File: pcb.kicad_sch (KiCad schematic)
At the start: 23 parts, among them SW1 SW_Push, SW2 SW_Push, U1 Pico

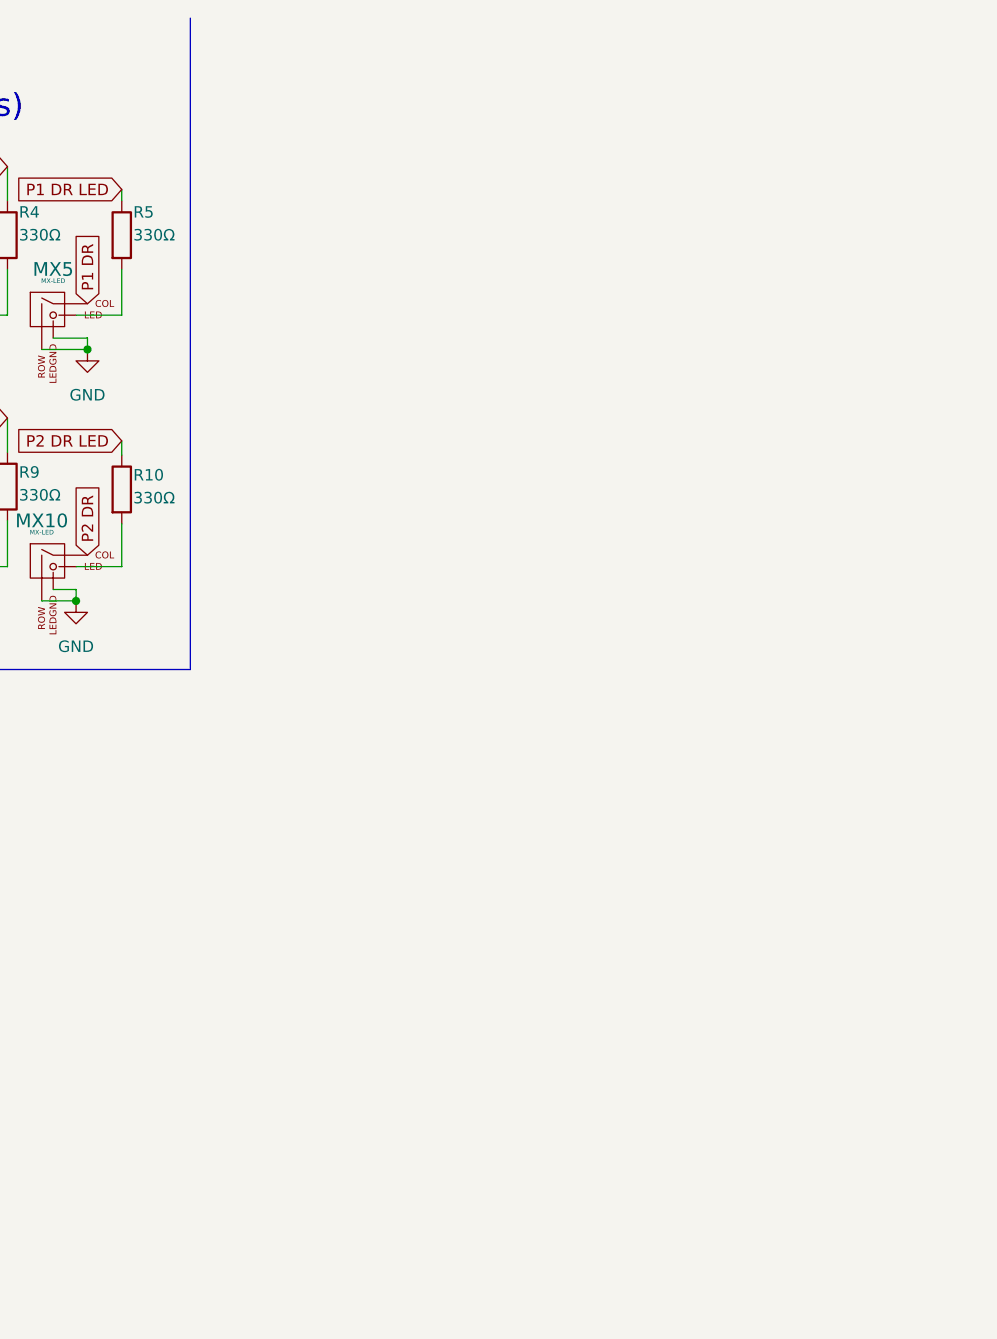
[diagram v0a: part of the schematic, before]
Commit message: Add WS2812B footprints, various tweaks
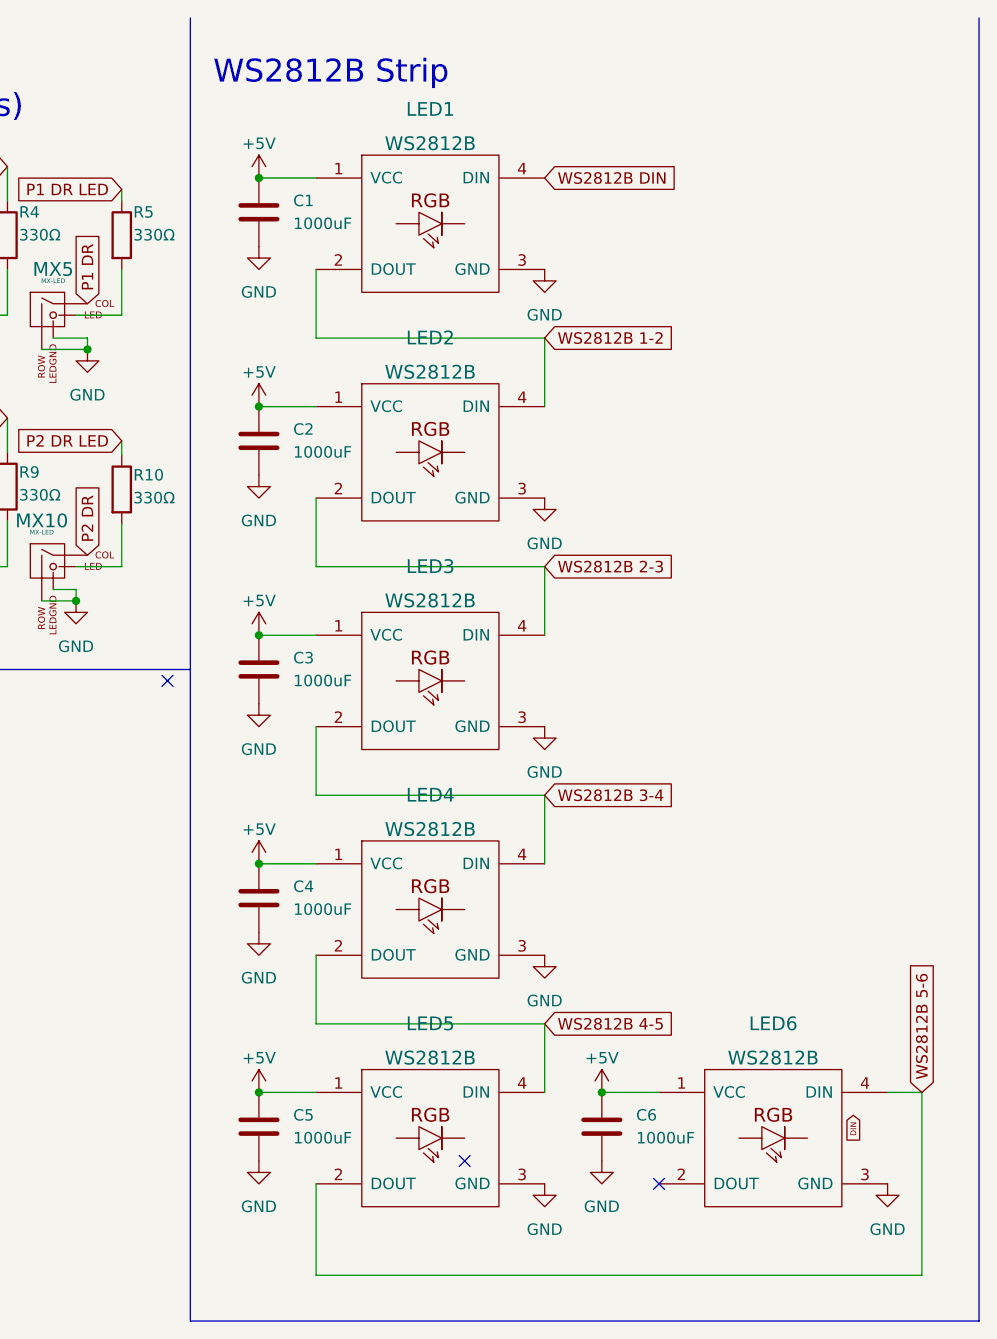
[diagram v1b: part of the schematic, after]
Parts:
- added C1, C2, C3, C4, C5, C6: 1000uF, Capacitor_SMD:C_0805_2012Metric_Pad1.18x1.45mm_HandSolder, symbol Device:C
- added LED1, LED2, LED3, LED4, LED5, LED6: WS2812B, LED_SMD:LED_WS2812B_PLCC4_5.0x5.0mm_P3.2mm, symbol ws2812b:WS2812B
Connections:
- net +5V: now also C1.1, C2.1, C3.1, C4.1, C5.1, C6.1, LED1.1 (VCC), LED2.1 (VCC), LED3.1 (VCC), LED4.1 (VCC), LED5.1 (VCC), LED6.1 (VCC)
- net GND: now also C1.2, C2.2, C3.2, C4.2, C5.2, C6.2, LED1.3 (GND), LED2.3 (GND), LED3.3 (GND), LED4.3 (GND), LED5.3 (GND), LED6.3 (GND)
- net WS2812B DIN: now also LED1.4 (DIN)
- new net WS2812B 1-2: LED1.2 (DOUT), LED2.4 (DIN)
- new net WS2812B 2-3: LED2.2 (DOUT), LED3.4 (DIN)
- new net WS2812B 3-4: LED3.2 (DOUT), LED4.4 (DIN)
- new net WS2812B 4-5: LED4.2 (DOUT), LED5.4 (DIN)
- new net WS2812B 5-6: LED5.2 (DOUT), LED6.4 (DIN)
- no-connect marks 13 -> 16
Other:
- note added: "WS2812B Strip"

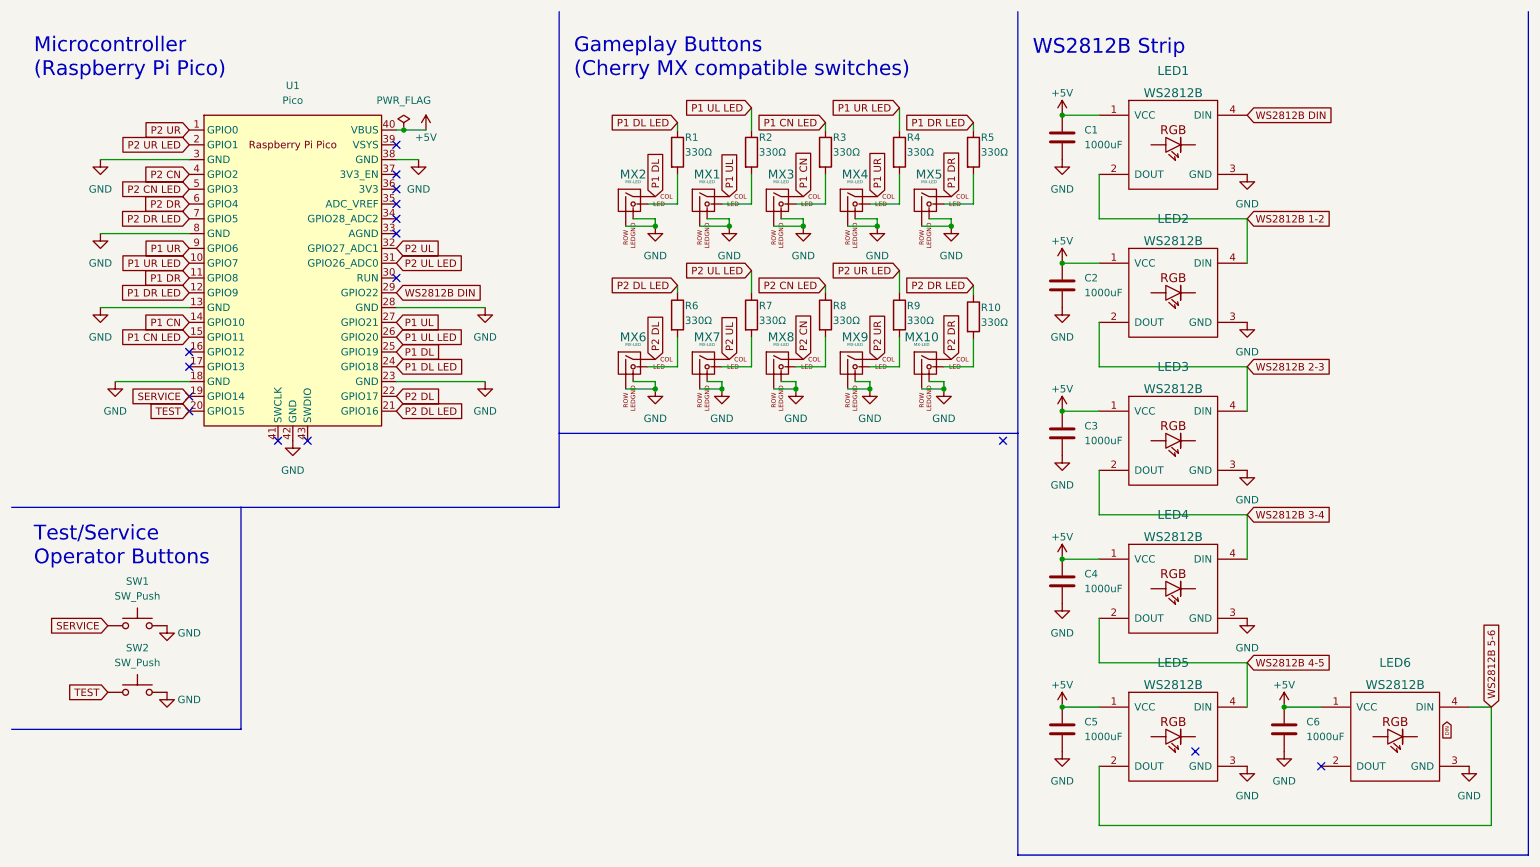
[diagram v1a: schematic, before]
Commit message: Fix P1 UL/DL being swapped
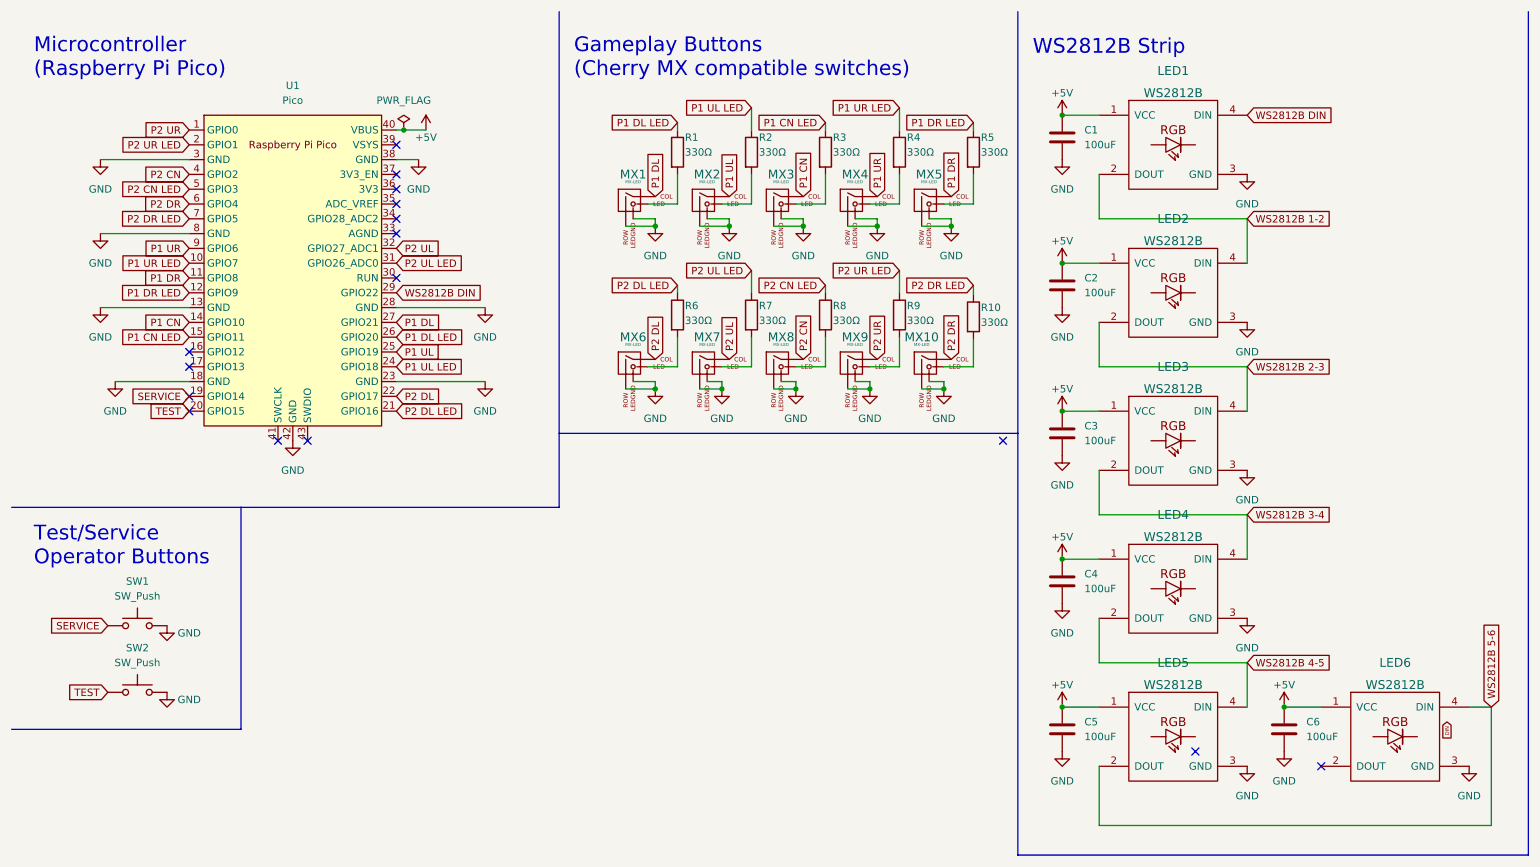
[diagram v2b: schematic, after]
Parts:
- C1, C2, C3, C4, C5, C6: value 1000uF -> 100uF
- LED1, LED2, LED3, LED4, LED5, LED6: LCSC (none) -> C2761795
- R1, R10, R2, R3, R4, R5, R6, R7, R8, R9: LCSC (none) -> C17630
- renumbered MX2 to MX1, MX1 to MX2
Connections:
- net P1 DL: now also U1.27 (GPIO21); no longer U1.25 (GPIO19)
- net P1 DL LED: now also U1.26 (GPIO20); no longer U1.24 (GPIO18)
- net P1 UL: now also U1.25 (GPIO19); no longer U1.27 (GPIO21)
- net P1 UL LED: now also U1.24 (GPIO18); no longer U1.26 (GPIO20)

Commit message: Add keeb.io Alps+Choc+MX footprint
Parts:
- MX1, MX10, MX2, MX3, MX4, MX5, MX6, MX7, MX8, MX9: footprint MX_Only:MXOnly-1U -> Keebio-Parts:MX-Alps-Choc-1U
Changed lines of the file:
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@@
       (effects (font (size 0.508 0.508)))
     )
-    (property "Footprint" "MX_Only:MXOnly-1U" (id 2) (at 126.365 43.815 0)
+    (property "Footprint" "Keebio-Parts:MX-Alps-Choc-1U" (id 2) (at 126.365 43.815 0)
       (effects (font (size 1.524 1.524)) hide)
     )
@@
       (effects (font (size 0.508 0.508)))
     )
-    (property "Footprint" "MX_Only:MXOnly-1U" (id 2) (at 113.665 71.755 0)
+    (property "Footprint" "Keebio-Parts:MX-Alps-Choc-1U" (id 2) (at 113.665 71.755 0)
       (effects (font (size 1.524 1.524)) hide)
     )
@@
       (effects (font (size 0.508 0.508)))
     )
-    (property "Footprint" "MX_Only:MXOnly-1U" (id 2) (at 139.065 71.755 0)
+    (property "Footprint" "Keebio-Parts:MX-Alps-Choc-1U" (id 2) (at 139.065 71.755 0)
       (effects (font (size 1.524 1.524)) hide)
     )
@@
       (effects (font (size 0.508 0.508)))
     )
-    (property "Footprint" "MX_Only:MXOnly-1U" (id 2) (at 151.765 43.815 0)
+    (property "Footprint" "Keebio-Parts:MX-Alps-Choc-1U" (id 2) (at 151.765 43.815 0)
       (effects (font (size 1.524 1.524)) hide)
     )
@@
       (effects (font (size 0.508 0.508)))
     )
-    (property "Footprint" "MX_Only:MXOnly-1U" (id 2) (at 113.665 43.815 0)
+    (property "Footprint" "Keebio-Parts:MX-Alps-Choc-1U" (id 2) (at 113.665 43.815 0)
       (effects (font (size 1.524 1.524)) hide)
     )
@@
       (effects (font (size 0.508 0.508)))
     )
-    (property "Footprint" "MX_Only:MXOnly-1U" (id 2) (at 139.065 43.815 0)
+    (property "Footprint" "Keebio-Parts:MX-Alps-Choc-1U" (id 2) (at 139.065 43.815 0)
       (effects (font (size 1.524 1.524)) hide)
     )
@@
       (effects (font (size 0.508 0.508)))
     )
-    (property "Footprint" "MX_Only:MXOnly-1U" (id 2) (at 100.965 71.755 0)
+    (property "Footprint" "Keebio-Parts:MX-Alps-Choc-1U" (id 2) (at 100.965 71.755 0)
       (effects (font (size 1.524 1.524)) hide)
     )
@@
       (effects (font (size 0.508 0.508)))
     )
-    (property "Footprint" "MX_Only:MXOnly-1U" (id 2) (at 100.965 43.815 0)
+    (property "Footprint" "Keebio-Parts:MX-Alps-Choc-1U" (id 2) (at 100.965 43.815 0)
       (effects (font (size 1.524 1.524)) hide)
     )
@@
       (effects (font (size 0.508 0.508)))
     )
-    (property "Footprint" "MX_Only:MXOnly-1U" (id 2) (at 151.765 71.755 0)
+    (property "Footprint" "Keebio-Parts:MX-Alps-Choc-1U" (id 2) (at 151.765 71.755 0)
       (effects (font (size 1.524 1.524)) hide)
     )
@@
       (effects (font (size 0.508 0.508)))
     )
-    (property "Footprint" "MX_Only:MXOnly-1U" (id 2) (at 126.365 71.755 0)
+    (property "Footprint" "Keebio-Parts:MX-Alps-Choc-1U" (id 2) (at 126.365 71.755 0)
       (effects (font (size 1.524 1.524)) hide)
     )
@@
     )
     (path "/9b58b2b3-67cf-495f-b667-1ffb1ad1d5b8"
-      (reference "MX1") (unit 1) (value "MX-LED") (footprint "MX_Only:MXOnly-1U")
+      (reference "MX1") (unit 1) (value "MX-LED") (footprint "Keebio-Parts:MX-Alps-Choc-1U")
     )
     (path "/766fdfb3-db19-48c2-b779-b910c8a2ecfb"
-      (reference "MX2") (unit 1) (value "MX-LED") (footprint "MX_Only:MXOnly-1U")
+      (reference "MX2") (unit 1) (value "MX-LED") (footprint "Keebio-Parts:MX-Alps-Choc-1U")
     )
     (path "/0a212509-b99d-4c27-a7b8-116754ebdf67"
-      (reference "MX3") (unit 1) (value "MX-LED") (footprint "MX_Only:MXOnly-1U")
+      (reference "MX3") (unit 1) (value "MX-LED") (footprint "Keebio-Parts:MX-Alps-Choc-1U")
     )
     (path "/78e64fc1-c1e1-4345-a497-d1b849807ee4"
-      (reference "MX4") (unit 1) (value "MX-LED") (footprint "MX_Only:MXOnly-1U")
+      (reference "MX4") (unit 1) (value "MX-LED") (footprint "Keebio-Parts:MX-Alps-Choc-1U")
     )
     (path "/536a524e-0516-416a-9f6f-926f774c2cf8"
-      (reference "MX5") (unit 1) (value "MX-LED") (footprint "MX_Only:MXOnly-1U")
+      (reference "MX5") (unit 1) (value "MX-LED") (footprint "Keebio-Parts:MX-Alps-Choc-1U")
     )
     (path "/8a292752-b364-49e7-86b0-b59a11d1e51a"
-      (reference "MX6") (unit 1) (value "MX-LED") (footprint "MX_Only:MXOnly-1U")
+      (reference "MX6") (unit 1) (value "MX-LED") (footprint "Keebio-Parts:MX-Alps-Choc-1U")
     )
     (path "/1e1d7dc6-b41a-409a-bf45-fae7b6730171"
-      (reference "MX7") (unit 1) (value "MX-LED") (footprint "MX_Only:MXOnly-1U")
+      (reference "MX7") (unit 1) (value "MX-LED") (footprint "Keebio-Parts:MX-Alps-Choc-1U")
     )
     (path "/f03166d2-869e-43f3-9697-a4505fe31560"
-      (reference "MX8") (unit 1) (value "MX-LED") (footprint "MX_Only:MXOnly-1U")
+      (reference "MX8") (unit 1) (value "MX-LED") (footprint "Keebio-Parts:MX-Alps-Choc-1U")
     )
     (path "/46f77868-e63b-46ae-b810-eeaefd31eed7"
-      (reference "MX9") (unit 1) (value "MX-LED") (footprint "MX_Only:MXOnly-1U")
+      (reference "MX9") (unit 1) (value "MX-LED") (footprint "Keebio-Parts:MX-Alps-Choc-1U")
     )
     (path "/cda60508-e18b-4fc3-b5b3-8870ee6e8fe9"
-      (reference "MX10") (unit 1) (value "MX-LED") (footprint "MX_Only:MXOnly-1U")
+      (reference "MX10") (unit 1) (value "MX-LED") (footprint "Keebio-Parts:MX-Alps-Choc-1U")
     )
     (path "/b6324ff8-d31b-40e8-8aa8-3b3c6d5e2e20"
